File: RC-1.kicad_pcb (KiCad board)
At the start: 2 copper layers, 38 x 22 mm, 9 parts, among them U1 STM32F401CEUx, U2 ADF7021

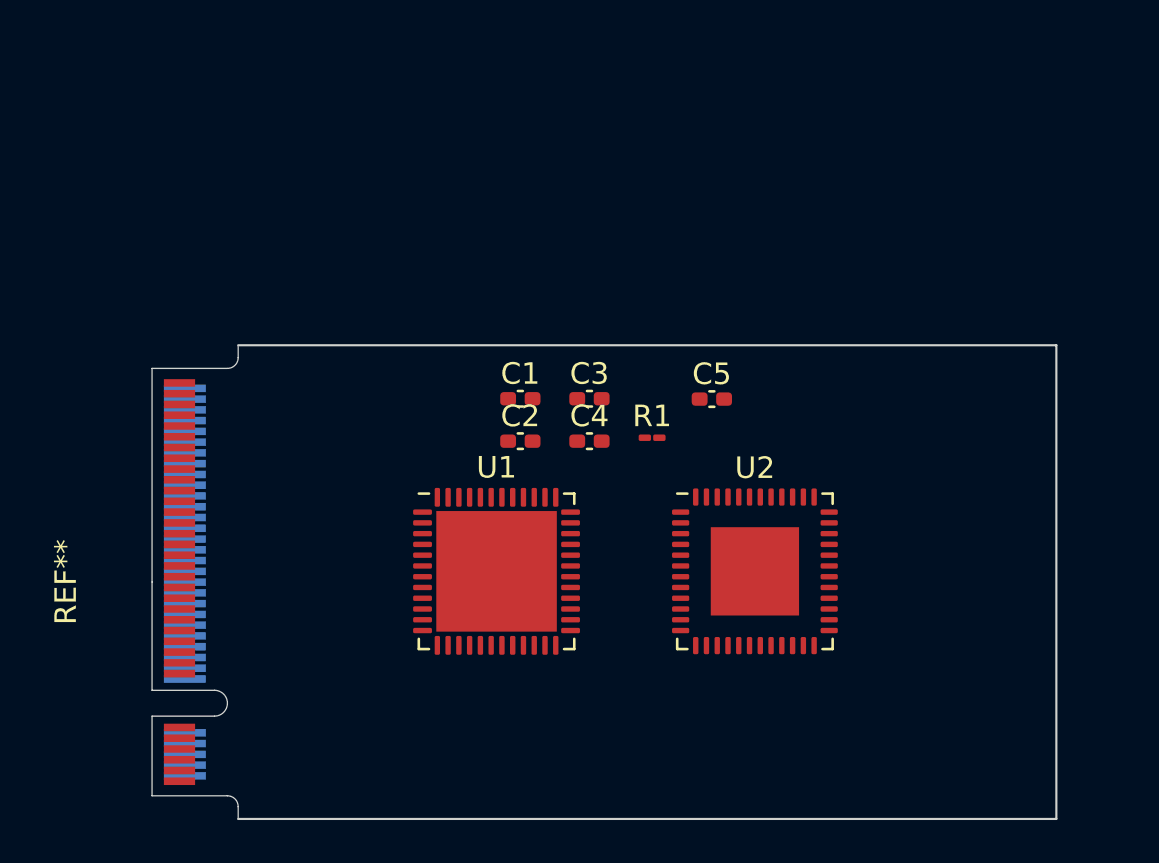
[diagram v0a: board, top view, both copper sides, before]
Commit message: Add old changes from 3 Aug 2021
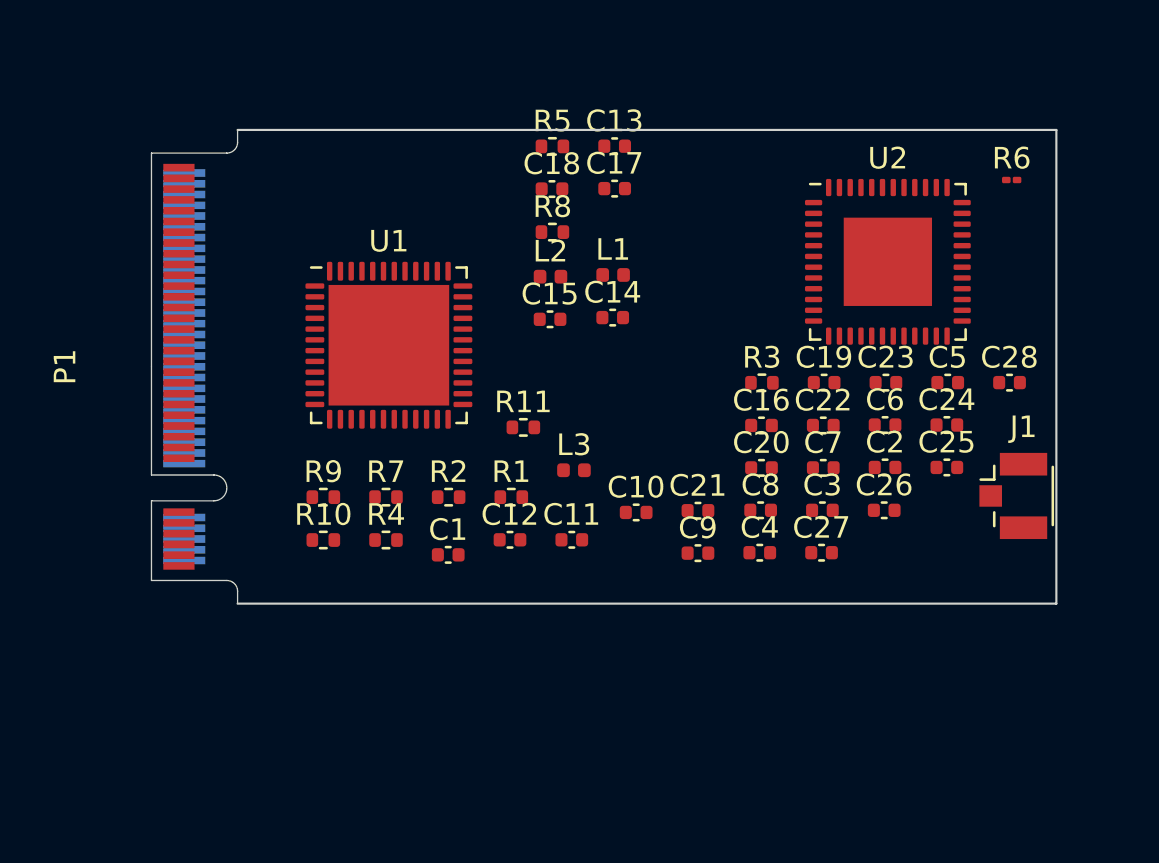
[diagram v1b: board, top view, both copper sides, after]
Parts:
- removed REF**: NGFF_B, NGFF:NGFF_B
- added C10: 100p, Capacitor_SMD:C_0402_1005Metric, F.Cu at (162.5, 87.8)
- added C11: 100n, Capacitor_SMD:C_0402_1005Metric, F.Cu at (159.5, 89.0)
- added C12: 100n, Capacitor_SMD:C_0402_1005Metric, F.Cu at (156.6, 89.0)
- added C13: 100n, Capacitor_SMD:C_0402_1005Metric, F.Cu at (161.5, 70.8)
- added C14: 22n, Capacitor_SMD:C_0402_1005Metric, F.Cu at (161.4, 78.7)
- added C15: 10n, Capacitor_SMD:C_0402_1005Metric, F.Cu at (158.5, 78.8)
- added C16: ?, Capacitor_SMD:C_0402_1005Metric, F.Cu at (168.3, 83.7)
- added C17: 470p, Capacitor_SMD:C_0402_1005Metric, F.Cu at (161.5, 72.7)
- added C18: 15n, Capacitor_SMD:C_0402_1005Metric, F.Cu at (158.6, 72.7)
- added C19: ?, Capacitor_SMD:C_0402_1005Metric, F.Cu at (171.2, 81.7)
- added C20: 1n, Capacitor_SMD:C_0402_1005Metric, F.Cu at (168.3, 85.7)
- added C21: ?, Capacitor_SMD:C_0402_1005Metric, F.Cu at (165.4, 87.7)
- added C22: 100n, Capacitor_SMD:C_0402_1005Metric, F.Cu at (171.2, 83.7)
- added C23: 10n, Capacitor_SMD:C_0402_1005Metric, F.Cu at (174.1, 81.7)
- added C24: ?, Capacitor_SMD:C_0402_1005Metric, F.Cu at (176.9, 83.7)
- added C25: 22n, Capacitor_SMD:C_0402_1005Metric, F.Cu at (176.9, 85.7)
- added C26: 100n, Capacitor_SMD:C_0402_1005Metric, F.Cu at (174.0, 87.7)
- added C27: 10n, Capacitor_SMD:C_0402_1005Metric, F.Cu at (171.1, 89.6)
- added C28: 10n, Capacitor_SMD:C_0402_1005Metric, F.Cu at (179.8, 81.7)
- added C6: 6p8, Capacitor_SMD:C_0402_1005Metric, F.Cu at (174.0, 83.7)
- added C7: 100n, Capacitor_SMD:C_0402_1005Metric, F.Cu at (171.2, 85.7)
- added C8: 100n, Capacitor_SMD:C_0402_1005Metric, F.Cu at (168.3, 87.7)
- added C9: 10n, Capacitor_SMD:C_0402_1005Metric, F.Cu at (165.4, 89.7)
- added J1: U.FL, Connector_Coaxial:U.FL_Hirose_U.FL-R-SMT-1_Vertical, F.Cu at (180.0, 87.0)
- added L1: 22n, Inductor_SMD:L_0402_1005Metric, F.Cu at (161.4, 76.7)
- added L2: 20n, Inductor_SMD:L_0402_1005Metric, F.Cu at (158.5, 76.8)
- added L3: 27n, Inductor_SMD:L_0402_1005Metric, F.Cu at (159.6, 85.8)
- added P1: PCIe_M.2_B-Key, NGFF:NGFF_B, F.Cu at (140.0, 81.0)
- added R10: 40K, Resistor_SMD:R_0402_1005Metric, F.Cu at (148.0, 89.0)
- added R11: 40K, Resistor_SMD:R_0402_1005Metric, F.Cu at (157.2, 83.8)
- added R2: 3r9, Resistor_SMD:R_0402_1005Metric, F.Cu at (153.8, 87.1)
- added R3: 3k6, Resistor_SMD:R_0402_1005Metric, F.Cu at (168.3, 81.7)
- added R4: 560, Resistor_SMD:R_0402_1005Metric, F.Cu at (150.9, 89.0)
- added R5: 270, Resistor_SMD:R_0402_1005Metric, F.Cu at (158.6, 70.8)
- added R6: R, Resistor_SMD:R_01005_0402Metric, F.Cu at (179.9, 72.3)
- added R7: 1K, Resistor_SMD:R_0402_1005Metric, F.Cu at (150.9, 87.1)
- added R8: 1K, Resistor_SMD:R_0402_1005Metric, F.Cu at (158.6, 74.7)
- added R9: 1K, Resistor_SMD:R_0402_1005Metric, F.Cu at (148.0, 87.1)
- C1: value 100n -> 6p8; footprint Capacitor_SMD:C_0402_1005Metric_Pad0.74x0.62mm_HandSolder -> Capacitor_SMD:C_0402_1005Metric
- C2, C3: footprint Capacitor_SMD:C_0402_1005Metric_Pad0.74x0.62mm_HandSolder -> Capacitor_SMD:C_0402_1005Metric
- C4: value 20p -> 10p; footprint Capacitor_SMD:C_0402_1005Metric_Pad0.74x0.62mm_HandSolder -> Capacitor_SMD:C_0402_1005Metric
- C5: value 20p -> 4p7; footprint Capacitor_SMD:C_0402_1005Metric_Pad0.74x0.62mm_HandSolder -> Capacitor_SMD:C_0402_1005Metric
- R1: value R -> 1k1; footprint Resistor_SMD:R_01005_0402Metric_Pad0.57x0.30mm_HandSolder -> Resistor_SMD:R_0402_1005Metric
- moved C2 17.0 mm to (174.0, 85.7)
- moved U2 15.6 mm to (174.2, 76.1)
- moved C3 12.0 mm to (171.1, 87.7)
- moved U1 11.6 mm to (151.0, 80.0)
- moved C5 11.0 mm to (177.0, 81.7)
- moved C4 9.46 mm to (168.2, 89.6)
- moved C1 7.99 mm to (153.8, 89.7)
- moved R1 7.10 mm to (156.7, 87.1)
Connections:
- C1 pad 1: VDD -> Net-(C1-Pad1)
- C2 pad 1: VDD -> Net-(C2-Pad1)
- C2 pad 2: GND -> RF
- C3 pad 1: VDD -> Net-(AE1-Pad2)
- C3 pad 2: GND -> RF
- C4 pad 1: OSC_IN -> Net-(C4-Pad1)
- C4 pad 2: GND -> Net-(C4-Pad2)
- C5 pad 1: Net-(C5-Pad1) -> Net-(C4-Pad1)
- C5 pad 2: GND -> Net-(C5-Pad2)
- R1 pad 1: OSC_OUT -> Net-(R1-Pad1)
- R1 pad 2: Net-(C5-Pad1) -> GND
- U1 pad 18: Net-(U1-Pad18) -> CE
- U1 pad 21: Net-(U1-Pad21) -> DATAIN
- U1 pad 25: Net-(U1-Pad25) -> DATAOUT
- U1 pad 3: CE -> OSC32_IN
- U1 pad 31: Net-(U1-Pad31) -> M2_LED
- U1 pad 32: Net-(U1-Pad32) -> USB_D-
- U1 pad 33: Net-(U1-Pad33) -> USB_D+
- U1 pad 34: Net-(U1-Pad34) -> W_DISABLE
- U1 pad 37: Net-(U1-Pad37) -> POWEROFF
- U1 pad 4: Net-(U1-Pad4) -> OSC32_OUT
- U1 pad 46: Net-(U1-Pad46) -> CLKOUT
- U1 pad 7: Net-(U1-Pad7) -> RESET#
- U2 pad 12: Net-(U2-Pad12) -> GND
- U2 pad 19: Net-(U2-Pad19) -> GND
- U2 pad 22: Net-(U2-Pad22) -> GND
- U2 pad 29: Net-(U2-Pad29) -> GND
- U2 pad 3: Net-(U2-Pad3) -> VDD
- U2 pad 32: Net-(U2-Pad32) -> VDD
- U2 pad 4: Net-(U2-Pad4) -> Net-(C4-Pad2)
- U2 pad 40: Net-(U2-Pad40) -> VDD
- U2 pad 43: Net-(U2-Pad43) -> VDD
- U2 pad 45: Net-(U2-Pad45) -> GND
- U2 pad 47: Net-(U2-Pad47) -> GND
- U2 pad 49: (no net) -> GND
- U2 pad 5: Net-(U2-Pad5) -> GND
- U2 pad 6: Net-(U2-Pad6) -> Net-(C5-Pad2)
- U2 pad 8: Net-(U2-Pad8) -> Net-(R1-Pad1)
- U2 pad 9: Net-(U2-Pad9) -> VDD

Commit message: Migrated project to Kicad 6.0, add gitignore to avoid committing backups
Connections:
- net I2S_OUT_SCK renamed I2S_SCK
- net I2S_OUT_SD renamed I2S_SD
- net I2S_OUT_WS renamed I2S_WS
- net Net-(P1-Pad26) renamed PTT
- net Net-(P1-Pad52) renamed AUDIO_IN
- net Net-(P1-Pad54) renamed AUDIO_OUT
- P1 pad 1: Net-(P1-Pad1) -> unconnected-(P1-Pad1)
- P1 pad 20: I2S_IN_SD -> SPI2_CS
- P1 pad 25: Net-(P1-Pad25) -> unconnected-(P1-Pad25)
- P1 pad 29: Net-(P1-Pad29) -> unconnected-(P1-Pad29)
- P1 pad 30: Net-(P1-Pad30) -> unconnected-(P1-Pad30)
- P1 pad 31: Net-(P1-Pad31) -> unconnected-(P1-Pad31)
- P1 pad 32: Net-(P1-Pad32) -> unconnected-(P1-Pad32)
- P1 pad 34: Net-(P1-Pad34) -> unconnected-(P1-Pad34)
- P1 pad 35: Net-(P1-Pad35) -> unconnected-(P1-Pad35)
- P1 pad 36: Net-(P1-Pad36) -> unconnected-(P1-Pad36)
- P1 pad 37: Net-(P1-Pad37) -> unconnected-(P1-Pad37)
- P1 pad 38: Net-(P1-Pad38) -> unconnected-(P1-Pad38)
- P1 pad 41: Net-(P1-Pad41) -> unconnected-(P1-Pad41)
- P1 pad 43: Net-(P1-Pad43) -> unconnected-(P1-Pad43)
- P1 pad 44: Net-(P1-Pad44) -> SPI2_SCLK
- P1 pad 46: I2S_IN_SCK -> SPI2_MISO
- P1 pad 47: Net-(P1-Pad47) -> unconnected-(P1-Pad47)
- P1 pad 48: I2S_IN_WS -> SPI2_MOSI
- P1 pad 49: Net-(P1-Pad49) -> unconnected-(P1-Pad49)
- P1 pad 50: Net-(P1-Pad50) -> unconnected-(P1-Pad50)
- P1 pad 53: Net-(P1-Pad53) -> unconnected-(P1-Pad53)
- P1 pad 55: Net-(P1-Pad55) -> unconnected-(P1-Pad55)
- P1 pad 56: Net-(P1-Pad56) -> unconnected-(P1-Pad56)
- P1 pad 58: Net-(P1-Pad58) -> unconnected-(P1-Pad58)
- P1 pad 59: SPI_SCLK -> SPI1_SCLK
- P1 pad 61: SPI_MISO -> SPI1_MISO
- P1 pad 63: SPI_MOSI -> SPI1_MOSI
- P1 pad 65: SPI_CS -> SPI1_CS
- P1 pad 66: Net-(P1-Pad66) -> unconnected-(P1-Pad66)
- P1 pad 68: Net-(P1-Pad68) -> unconnected-(P1-Pad68)
- P1 pad 69: Net-(P1-Pad69) -> unconnected-(P1-Pad69)
- U1 pad 10: Net-(U1-Pad10) -> unconnected-(U1-Pad10)
- U1 pad 11: Net-(U1-Pad11) -> unconnected-(U1-Pad11)
- U1 pad 12: Net-(U1-Pad12) -> unconnected-(U1-Pad12)
- U1 pad 13: Net-(U1-Pad13) -> unconnected-(U1-Pad13)
- U1 pad 14: Net-(U1-Pad14) -> SPI1_CS
- U1 pad 15: Net-(U1-Pad15) -> SPI1_SCLK
- U1 pad 16: Net-(U1-Pad16) -> SPI1_MISO
- U1 pad 17: Net-(U1-Pad17) -> SPI1_MOSI
- U1 pad 19: Net-(U1-Pad19) -> unconnected-(U1-Pad19)
- U1 pad 2: Net-(U1-Pad2) -> unconnected-(U1-Pad2)
- U1 pad 20: Net-(U1-Pad20) -> unconnected-(U1-Pad20)
- U1 pad 21: DATAIN -> unconnected-(U1-Pad21)
- U1 pad 22: Net-(U1-Pad22) -> unconnected-(U1-Pad22)
- U1 pad 25: DATAOUT -> SPI2_CS
- U1 pad 26: Net-(U1-Pad26) -> SPI2_SCLK
- U1 pad 27: Net-(U1-Pad27) -> SPI2_MISO
- U1 pad 28: Net-(U1-Pad28) -> SPI2_MOSI
- U1 pad 29: Net-(U1-Pad29) -> unconnected-(U1-Pad29)
- U1 pad 30: Net-(U1-Pad30) -> unconnected-(U1-Pad30)
- U1 pad 38: Net-(U1-Pad38) -> unconnected-(U1-Pad38)
- U1 pad 39: Net-(U1-Pad39) -> unconnected-(U1-Pad39)
- U1 pad 40: Net-(U1-Pad40) -> unconnected-(U1-Pad40)
- U1 pad 41: SCLK -> unconnected-(U1-Pad41)
- U1 pad 42: SDATA -> I2C_SCL
- U1 pad 43: SREAD -> I2C_SDA
- U1 pad 44: Net-(U1-Pad44) -> unconnected-(U1-Pad44)
- U1 pad 45: SLE -> unconnected-(U1-Pad45)
- U1 pad 46: CLKOUT -> unconnected-(U1-Pad46)
- U1 pad 9: Net-(U1-Pad9) -> unconnected-(U1-Pad9)
- U2 pad 13: Net-(U2-Pad13) -> unconnected-(U2-Pad13)
- U2 pad 14: Net-(U2-Pad14) -> unconnected-(U2-Pad14)
- U2 pad 15: Net-(U2-Pad15) -> unconnected-(U2-Pad15)
- U2 pad 16: Net-(U2-Pad16) -> unconnected-(U2-Pad16)
- U2 pad 17: Net-(U2-Pad17) -> unconnected-(U2-Pad17)
- U2 pad 18: Net-(U2-Pad18) -> unconnected-(U2-Pad18)
- U2 pad 20: Net-(U2-Pad20) -> unconnected-(U2-Pad20)
- U2 pad 21: Net-(U2-Pad21) -> unconnected-(U2-Pad21)
- U2 pad 23: Net-(U2-Pad23) -> unconnected-(U2-Pad23)
- U2 pad 30: Net-(U2-Pad30) -> unconnected-(U2-Pad30)
- U2 pad 33: Net-(U2-Pad33) -> unconnected-(U2-Pad33)
- U2 pad 37: Net-(U2-Pad37) -> unconnected-(U2-Pad37)
- U2 pad 38: Net-(U2-Pad38) -> unconnected-(U2-Pad38)
- U2 pad 44: Net-(U2-Pad44) -> unconnected-(U2-Pad44)
- U2 pad 46: Net-(U2-Pad46) -> unconnected-(U2-Pad46)
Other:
- net class Default removed

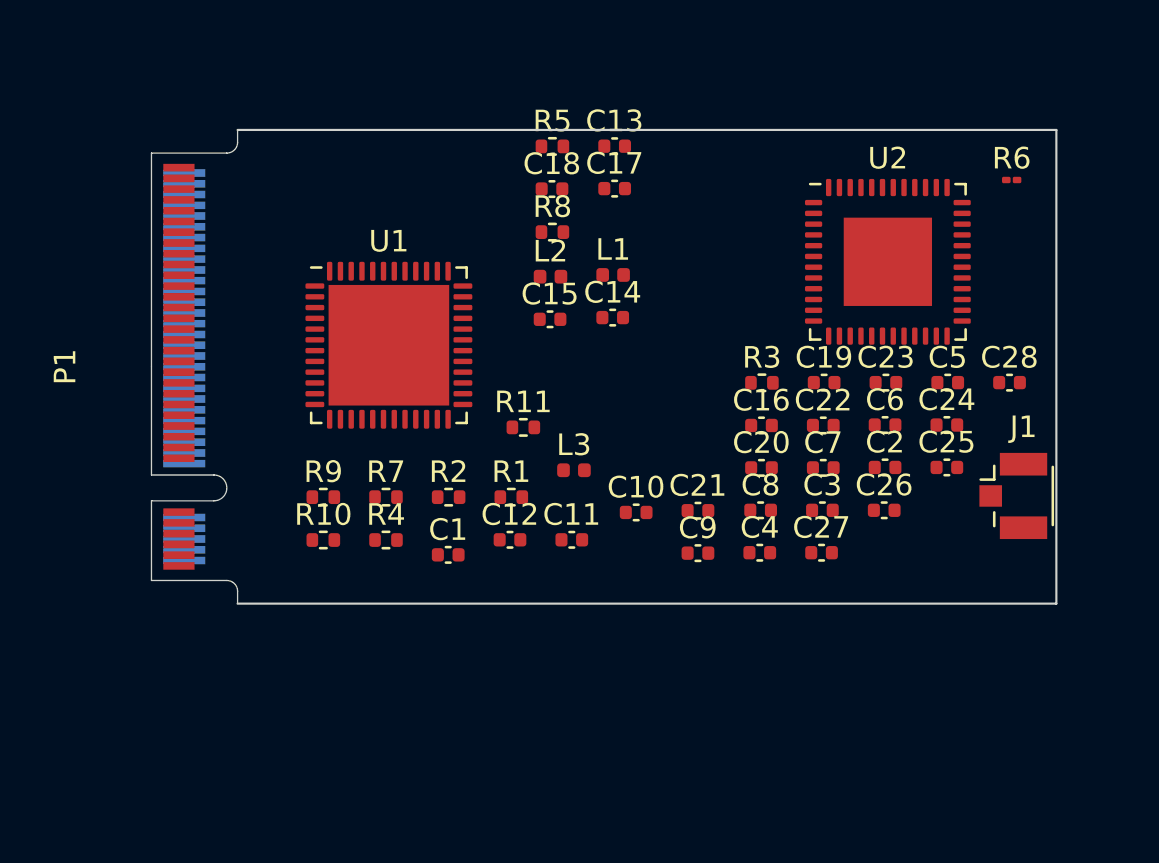
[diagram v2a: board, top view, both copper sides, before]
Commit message: Set up PCB for M.2 Type 3042-S3 form factor.
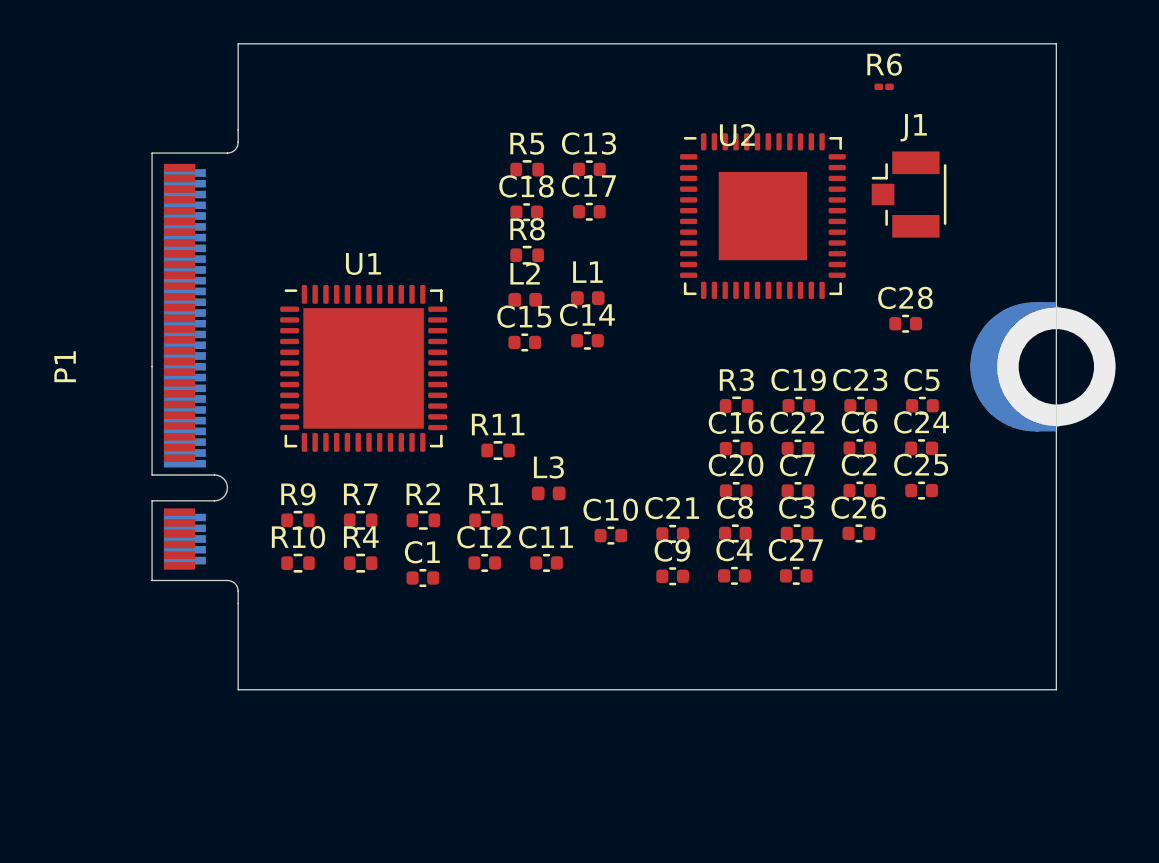
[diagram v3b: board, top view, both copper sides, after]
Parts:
- moved J1 14.9 mm to (175.0, 73.0)
- moved R6 7.34 mm to (174.0, 68.0)
- moved U2 6.18 mm to (168.4, 74.0)
- moved C28 5.55 mm to (175.0, 79.0)
- moved C10 1.59 mm to (161.3, 88.8)
- moved C11 1.59 mm to (158.3, 90.1)
- moved C12 1.59 mm to (155.4, 90.1)
- moved C13 1.59 mm to (160.3, 71.8)
- moved C14 1.59 mm to (160.2, 79.8)
- moved C15 1.59 mm to (157.3, 79.9)
- moved C19 1.59 mm to (170.0, 82.8)
- moved C2 1.59 mm to (172.9, 86.8)
- moved C23 1.59 mm to (172.9, 82.8)
- moved C5 1.59 mm to (175.8, 82.8)
- moved C6 1.59 mm to (172.9, 84.8)
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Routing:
- net GND: vias 0 -> 1
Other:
- board size 38 x 22 mm -> 38 x 30 mm
- copper layers 2 -> 4
- board text added: "M.2 Type 3042-S3"
